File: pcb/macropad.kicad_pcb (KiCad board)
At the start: 2 copper layers, 90 x 67 mm, 26 parts, among them J1 OLED_DISPLAY, SW1 SW_Push, SW2 SW_Push, SW3 SW_Push, SW4 SW_Push, SW5 RotaryEncoder_Switch, SW6 SW_Push, SW7 SW_Push, U1 Seeed Studio XIAO RP2040

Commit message: V1.4 - Reworked GND fields, solved all errors, added Steve
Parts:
- D11, D12, D13, D14, D15, D9: footprint Cherry-MX:MX_SK6812MINI-E -> Libraries:MX_SK6812MINI-E
- D7, D8: footprint LED_SMD:LED_SK6812MINI-E_3.2x2.8mm_P1.5mm_ReverseMount -> Libraries:SK6812MINI-E_fixed; moved to F.Cu
- U1: footprint Hackpad:XIAO-Generic-Hybrid-14P-2.54-21X17.8MM -> Libraries:XIAO-Generic-Hybrid-14P-2.54-21X17.8MM
- moved D7 0.70 mm to (170.5, 104.8)
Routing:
- net Net-(D12-DOUT): track 71.5 -> 81.2 mm
- net Row 1: track 96.3 -> 97.8 mm
- net VCC: track 375.7 -> 374.5 mm
- net SCL: track 67.5 -> 68.6 mm
- net Column 2: track 111.7 -> 111.1 mm
- net GND: vias 0 -> 24
- added copper zone on B.Cu, net GND
- added copper zone on F.Cu, net GND
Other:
- board size 90 x 67 mm -> 90 x 68 mm

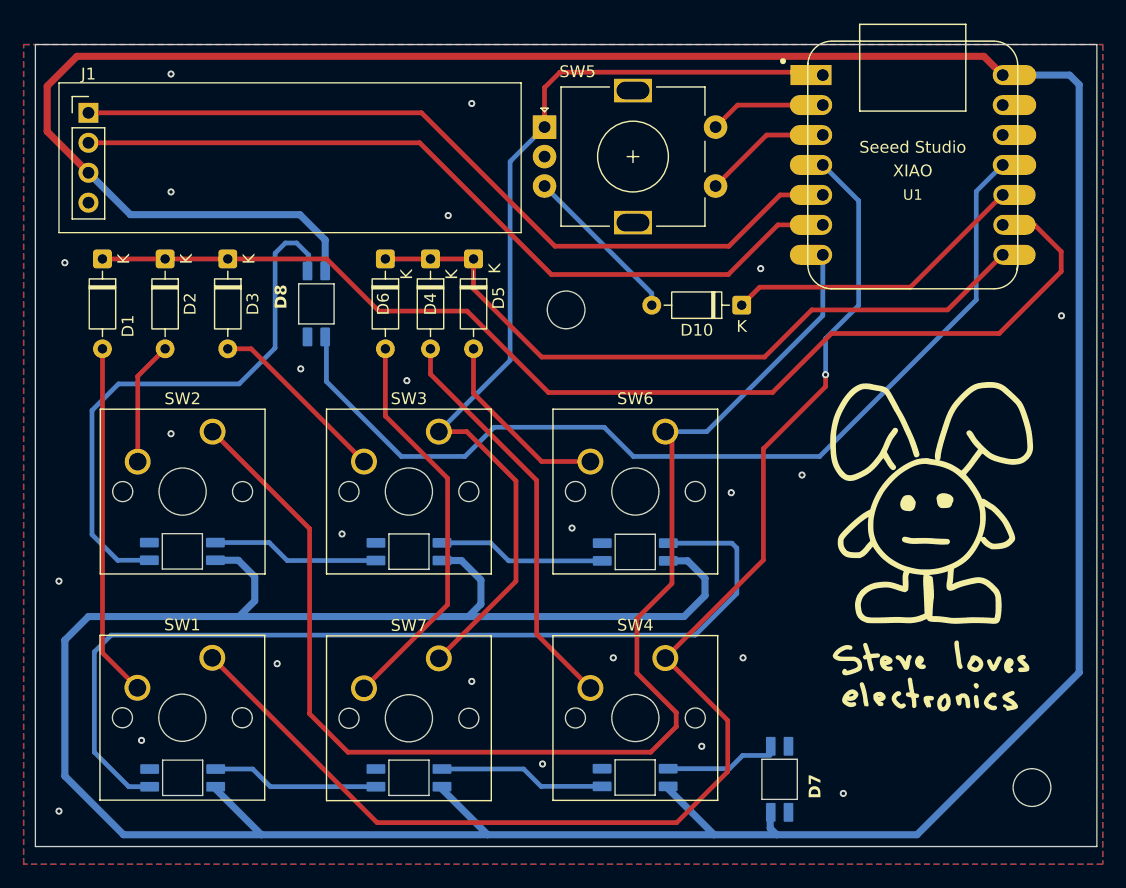
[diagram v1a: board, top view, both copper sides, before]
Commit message: Moved the KiCad libraries. Added the CAD case elements
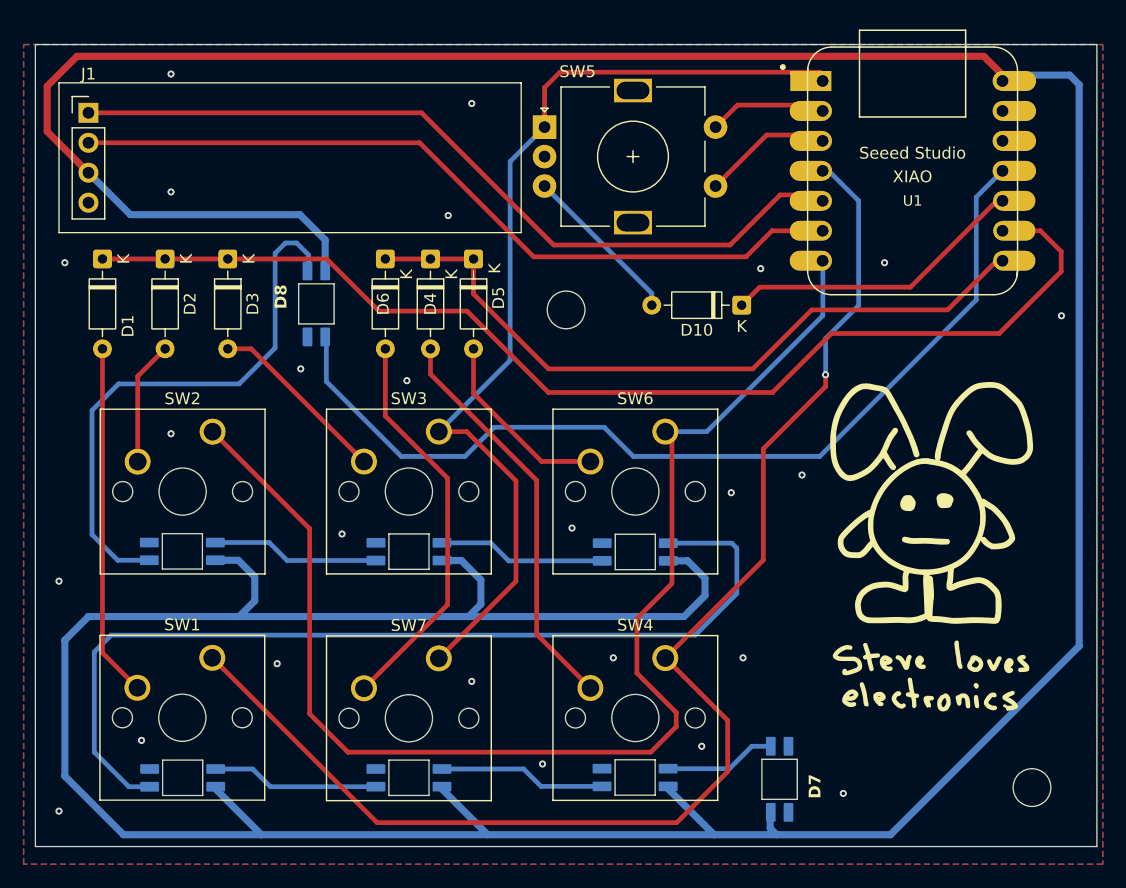
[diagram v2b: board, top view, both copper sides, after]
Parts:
- moved U1 0.50 mm to (181.9, 53.2)
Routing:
- net SCL: track 68.6 -> 67.2 mm
- net Row 2: track 60.9 -> 61.7 mm
- net VCC: track 374.5 -> 373.9 mm
- net GND: vias 24 -> 25

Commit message: V1.5 - Fixed faulty encoder wiring, retraced
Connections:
- SW5 pad A: Column 3 -> EN_A
- SW5 pad B: Net-(D10-A) -> EN_B
- SW5 pad S1: S1 -> Column 3
- SW5 pad S2: S2 -> Net-(D10-A)
- U1 pad 2: S2 -> EN_A
- U1 pad 3: S1 -> EN_B
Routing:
- net EN_A: track 0.00 -> 29.0 mm
- net EN_B: track 0.00 -> 25.2 mm
- net S1: track 11.1 -> 0.00 mm
- net S2: track 10.1 -> 0.00 mm
- net Net-(D10-A): track 13.9 -> 17.3 mm
- net Column 3: track 83.6 -> 85.3 mm
- net GND: vias 25 -> 27
